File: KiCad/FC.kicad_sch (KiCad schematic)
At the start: 12 parts, among them SW11 SW_SPST, SW12 SW_SPST, SW13 SW_SPST, SW14 SW_SPST, SW15 SW_SPST, SW16 SW_SPST

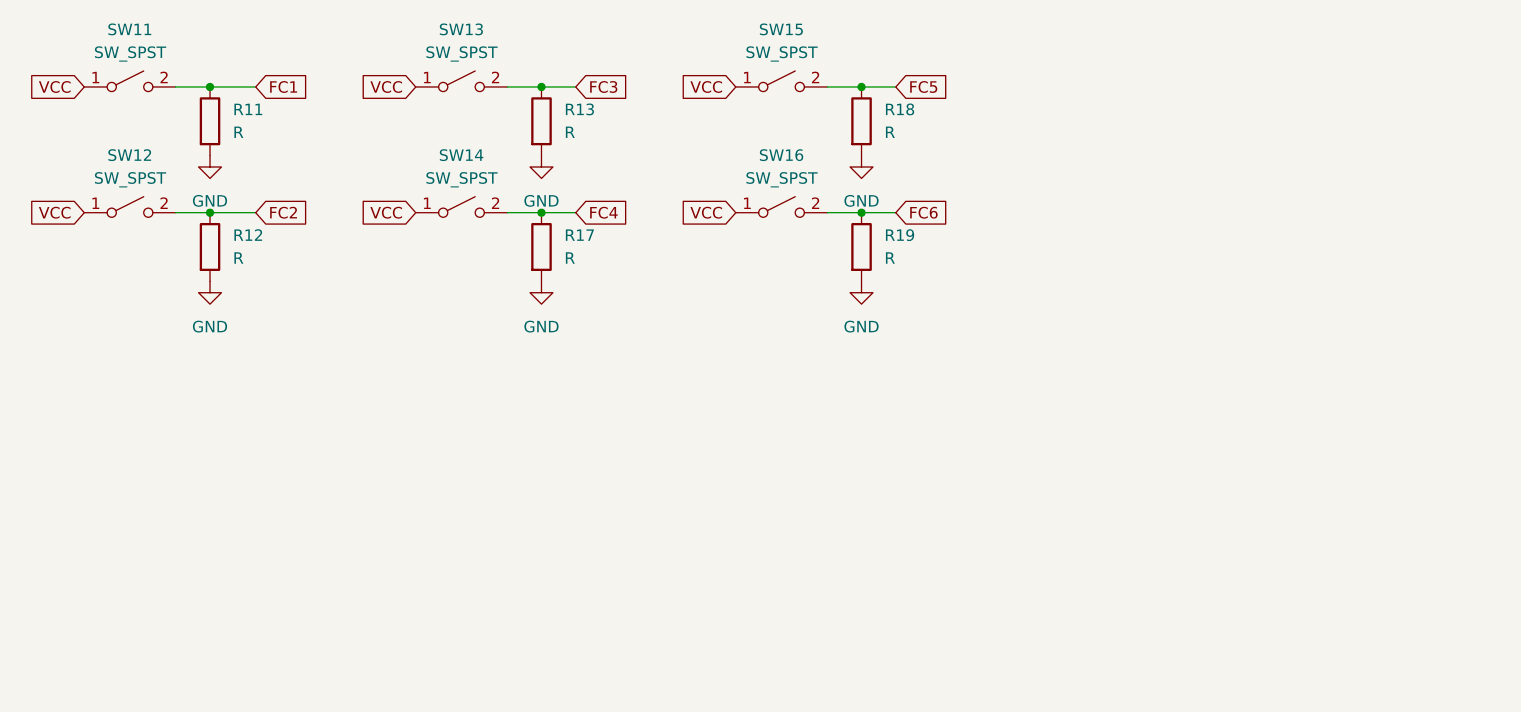
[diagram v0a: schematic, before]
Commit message: añadido conexiones del PIC y cambiado lógica de los drivers para reducir pines
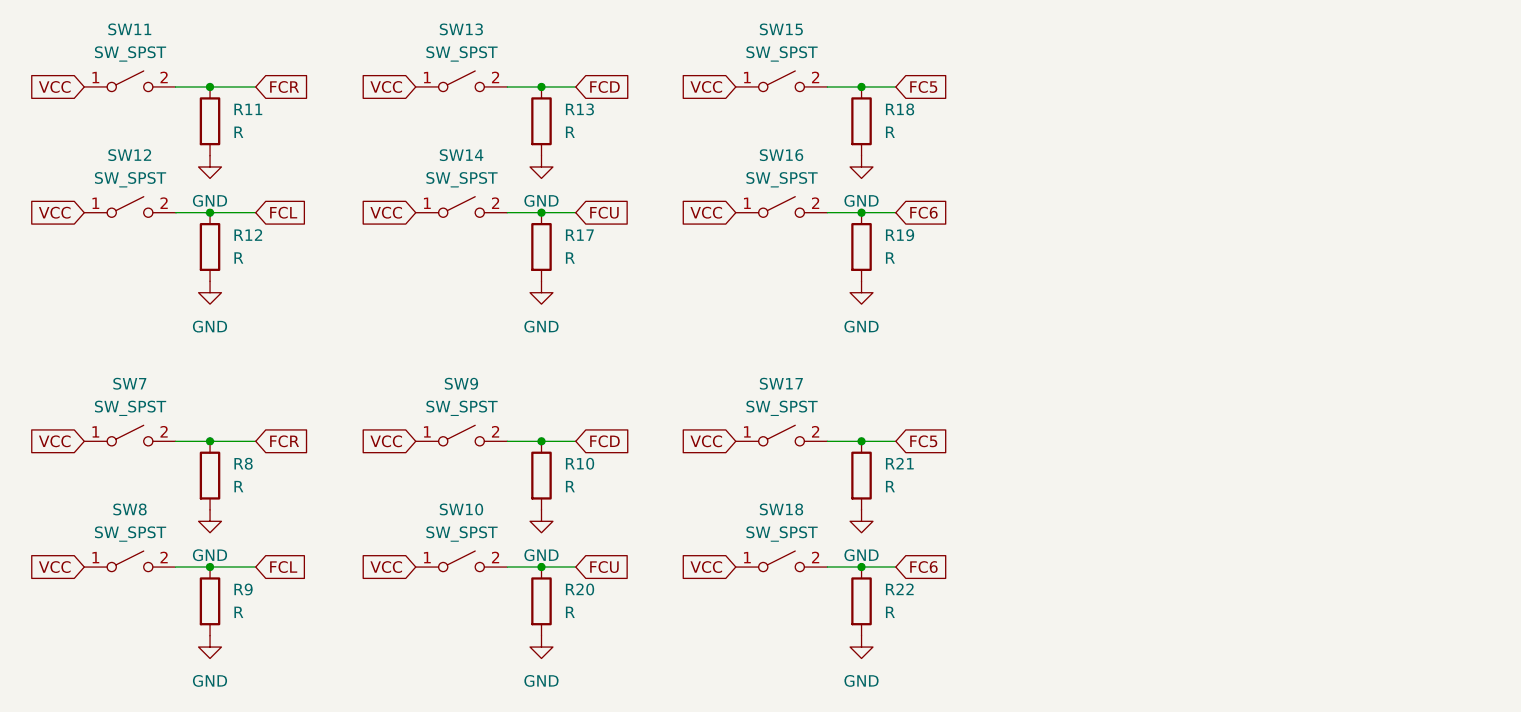
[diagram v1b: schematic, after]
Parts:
- added R10, R20, R21, R22, R8, R9: R, symbol Device:R
- added SW10, SW17, SW18, SW7, SW8, SW9: SW_SPST, symbol Switch:SW_SPST
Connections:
- net FC5: now also R21.1, SW17.2 (B)
- net FC6: now also R22.1, SW18.2 (B)
- net GND: now also R10.2, R20.2, R21.2, R22.2, R8.2, R9.2
- net VCC: now also SW10.1 (A), SW17.1 (A), SW18.1 (A), SW7.1 (A), SW8.1 (A), SW9.1 (A)
- net FC1 renamed FCR
- net FCR: now also R8.1, SW7.2 (B)
- net FC2 renamed FCL
- net FCL: now also R9.1, SW8.2 (B)
- net FC3 renamed FCD
- net FCD: now also R10.1, SW9.2 (B)
- net FC4 renamed FCU
- net FCU: now also R20.1, SW10.2 (B)

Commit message: reducido motores y finales de carrera
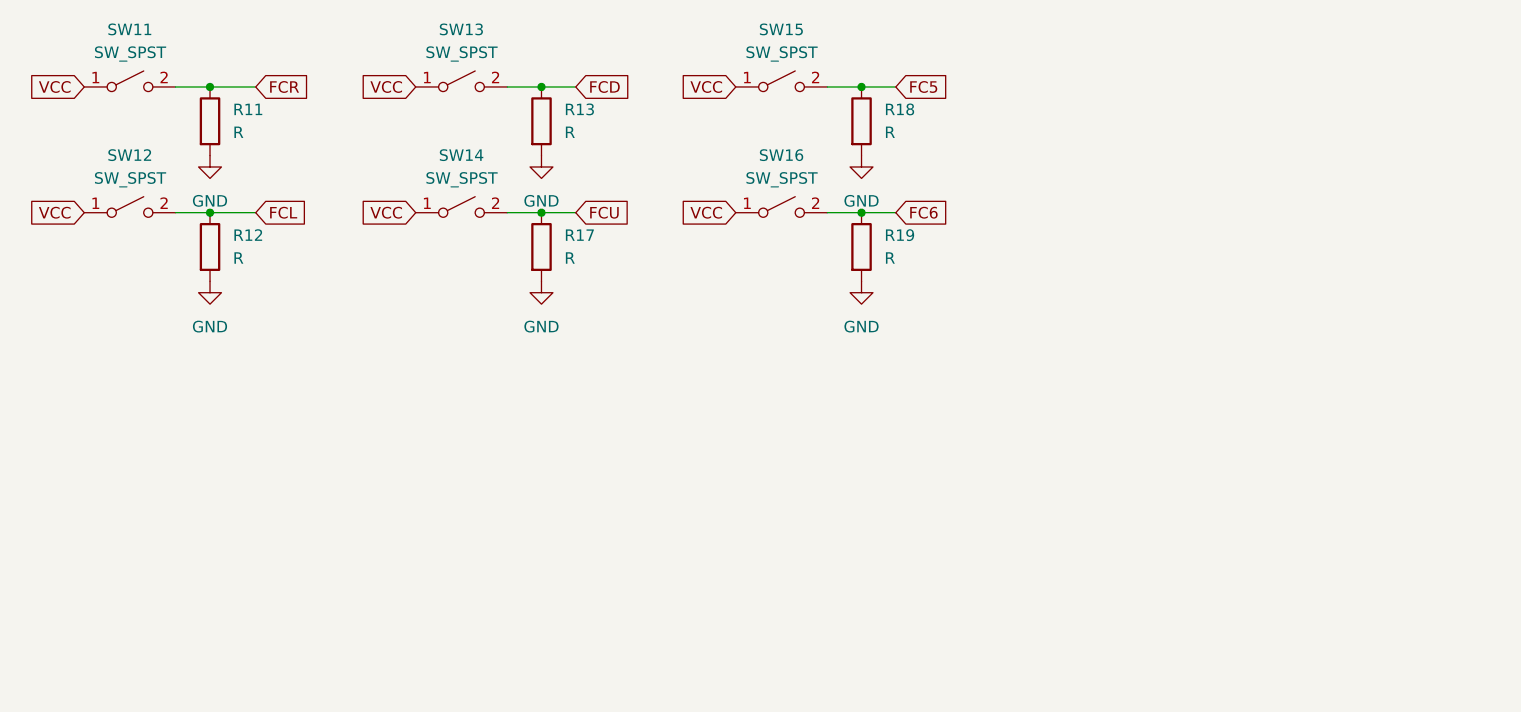
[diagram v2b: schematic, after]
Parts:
- removed R10, R20, R21, R22, R8, R9: R, symbol Device:R
- removed SW10, SW17, SW18, SW7, SW8, SW9: SW_SPST, symbol Switch:SW_SPST

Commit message: he añadido el resto de huellas, he corregido algunos errores en la parte de alimentación en los diodos. tambien he trasladados todas las huellas a la pcb y lo he intentado separar un poco para verlo mas claro cuando empecemos el placing.
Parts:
- R11, R12, R13, R17, R18, R19: footprint (none) -> Resistor_SMD:R_0402_1005Metric
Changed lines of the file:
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@@
 			)
 		)
-		(property "Footprint" ""
+		(property "Footprint" "Resistor_SMD:R_0402_1005Metric"
 			(at 174.752 97.79 90)
 			(effects
@@
 			)
 		)
-		(property "Footprint" ""
+		(property "Footprint" "Resistor_SMD:R_0402_1005Metric"
 			(at 139.192 83.82 90)
 			(effects
@@
 			)
 		)
-		(property "Footprint" ""
+		(property "Footprint" "Resistor_SMD:R_0402_1005Metric"
 			(at 102.362 97.79 90)
 			(effects
@@
 			)
 		)
-		(property "Footprint" ""
+		(property "Footprint" "Resistor_SMD:R_0402_1005Metric"
 			(at 102.362 83.82 90)
 			(effects
@@
 			)
 		)
-		(property "Footprint" ""
+		(property "Footprint" "Resistor_SMD:R_0402_1005Metric"
 			(at 174.752 83.82 90)
 			(effects
@@
 			)
 		)
-		(property "Footprint" ""
+		(property "Footprint" "Resistor_SMD:R_0402_1005Metric"
 			(at 139.192 97.79 90)
 			(effects

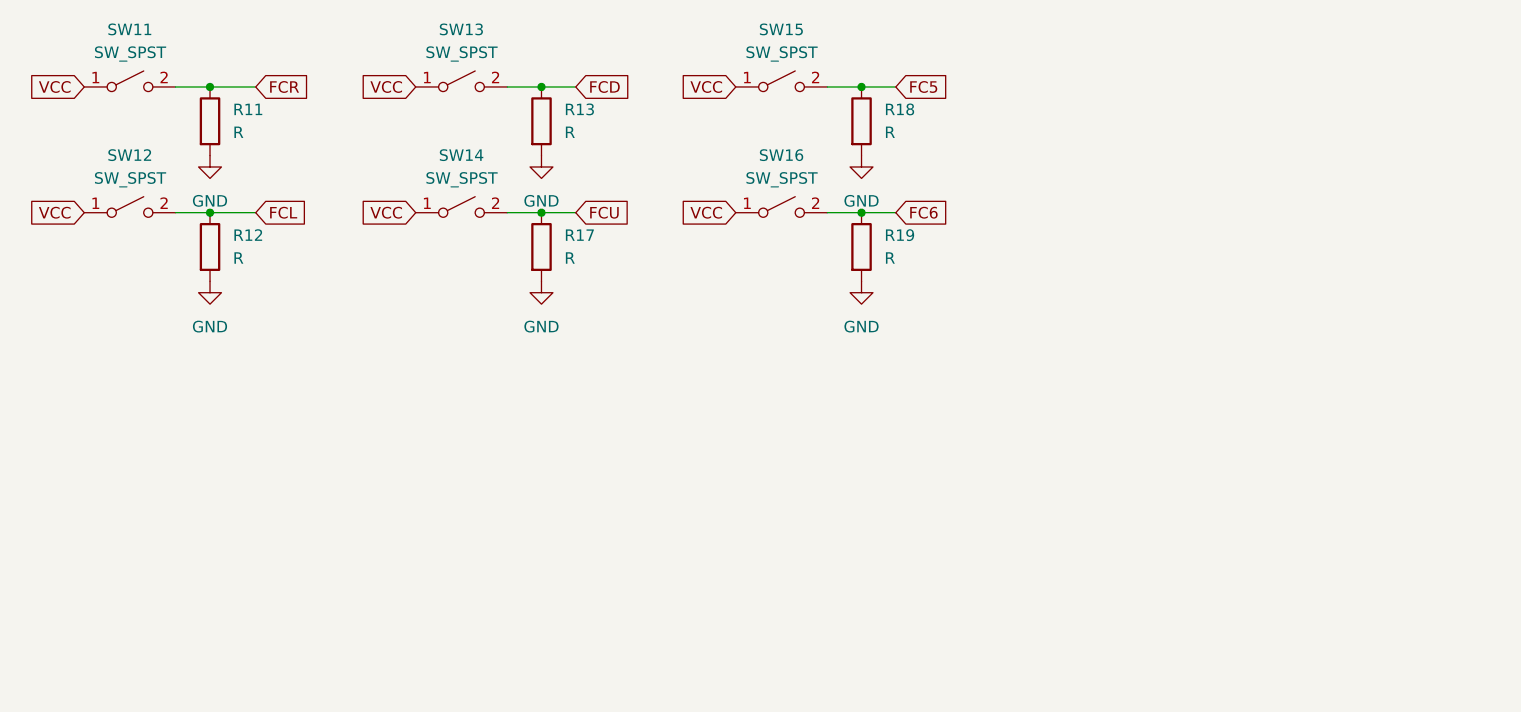
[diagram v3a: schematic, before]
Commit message: terminado placement (reorganizado pines del micro y añadido cambios de sensores/calefactor por conectores)
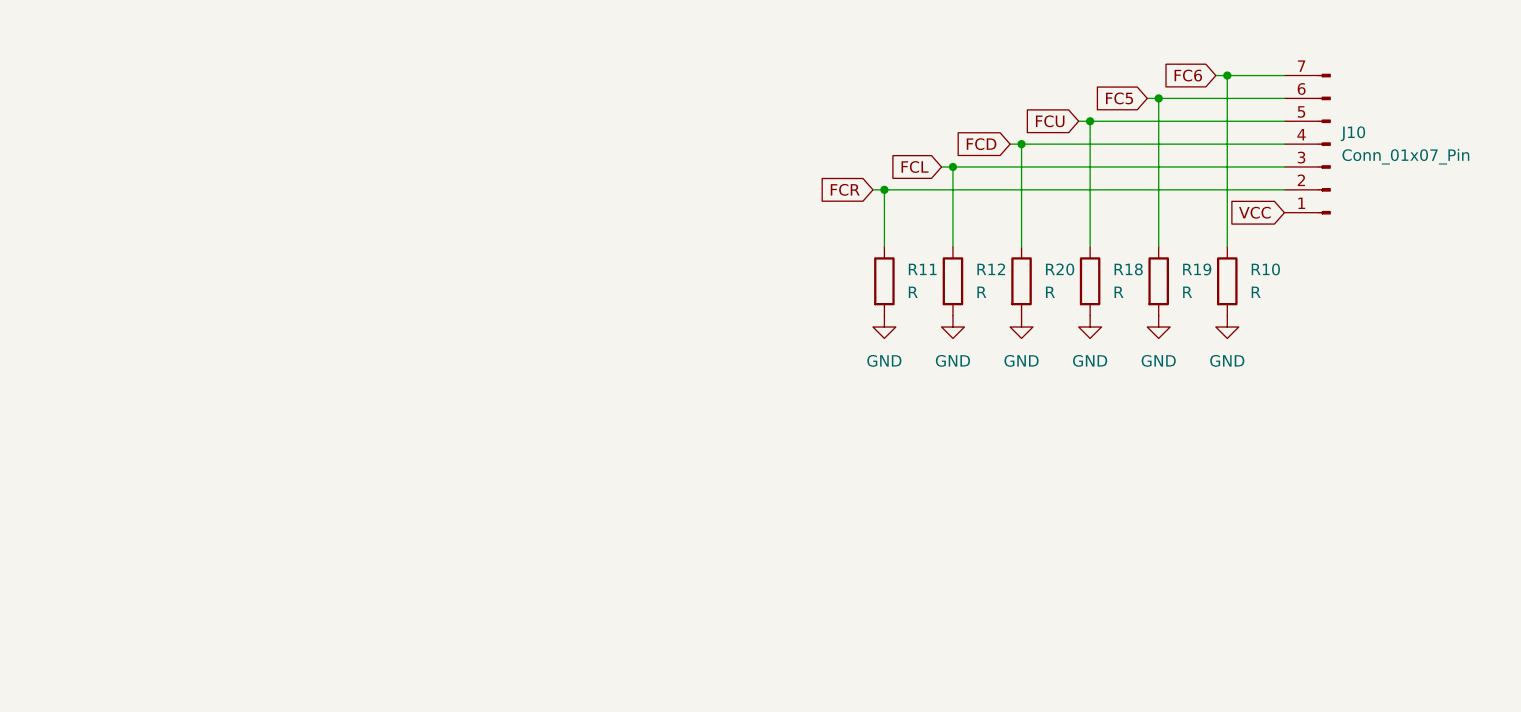
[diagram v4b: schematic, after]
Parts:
- removed R13, R17: R, Resistor_SMD:R_0402_1005Metric, symbol Device:R
- removed SW11, SW12, SW13, SW14, SW15, SW16: SW_SPST, symbol Switch:SW_SPST
- added J10: Conn_01x07_Pin, Connector_PinHeader_2.54mm:PinHeader_1x07_P2.54mm_Vertical, symbol Connector:Conn_01x07_Pin
- added R10, R20: R, Resistor_SMD:R_0402_1005Metric, symbol Device:R
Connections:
- net FC5: now also R19.1, J10.6 (Pin_6); no longer R18.1
- net FC6: now also J10.7 (Pin_7), R10.1; no longer R19.1
- net FCD: now also J10.4 (Pin_4), R20.1
- net FCL: now also J10.3 (Pin_3)
- net FCR: now also J10.2 (Pin_2)
- net FCU: now also R18.1, J10.5 (Pin_5)
- net GND: now also R10.2, R20.2
- net VCC: now also J10.1 (Pin_1)
